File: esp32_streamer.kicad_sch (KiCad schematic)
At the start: 46 parts, among them J1 USB4510-03-1-A, J2 SJ1-3533NS, J3 Conn_01x04_Male, U1 PCM5122PW, U2 ESP32-WROVER-EM213EH2864PH3Q0, U3 MCP1825S, U4 MCP1825S

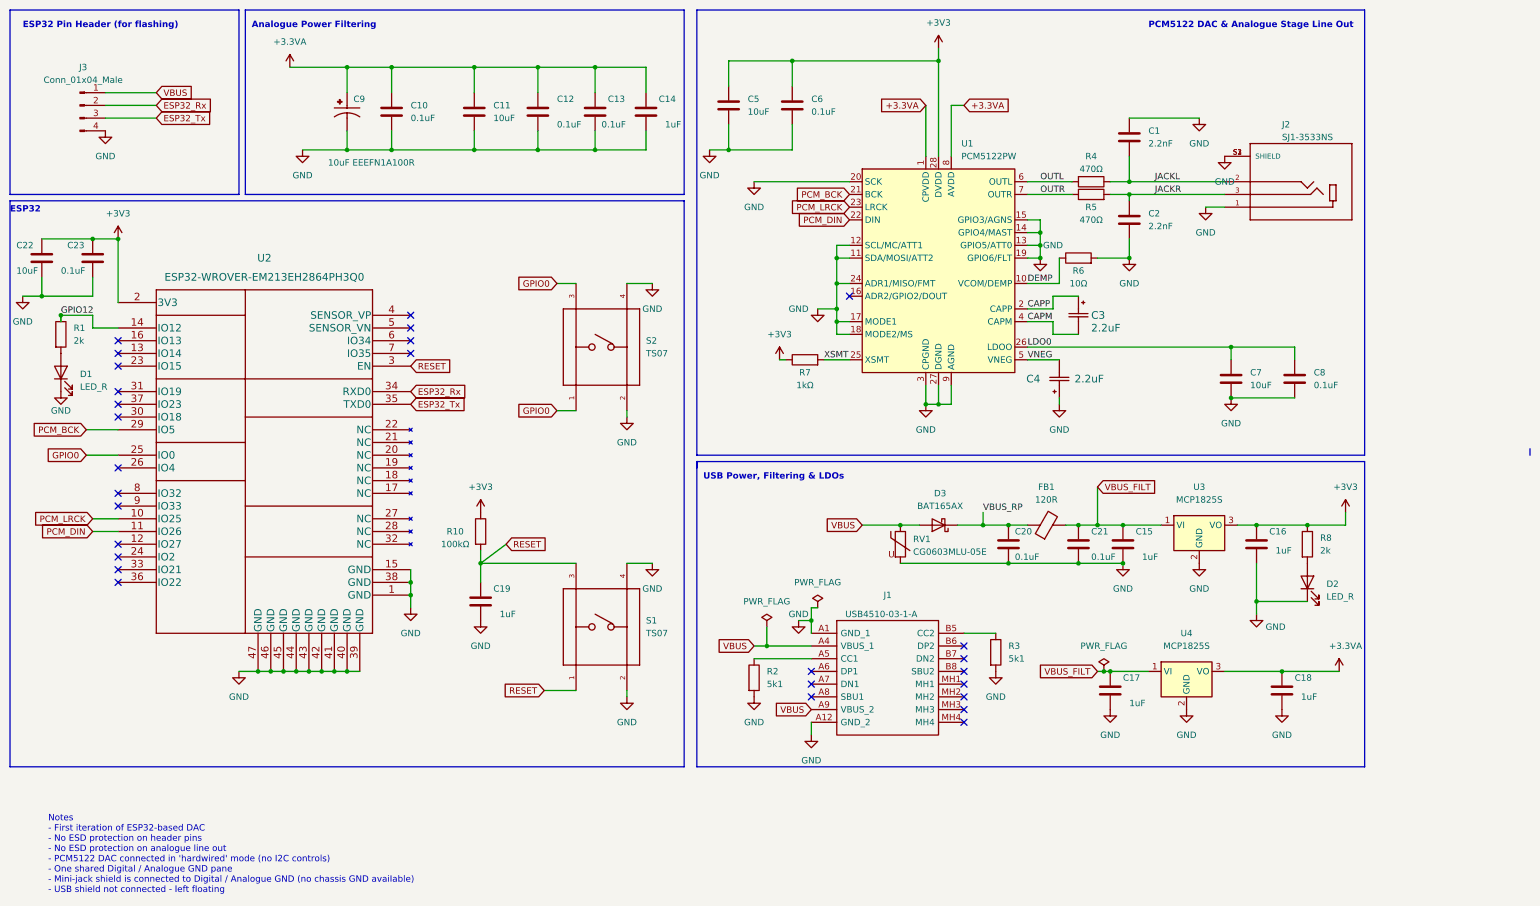
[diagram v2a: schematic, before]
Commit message: Updated PCB layout - now it looks cleaner - completed layout. next step: traces
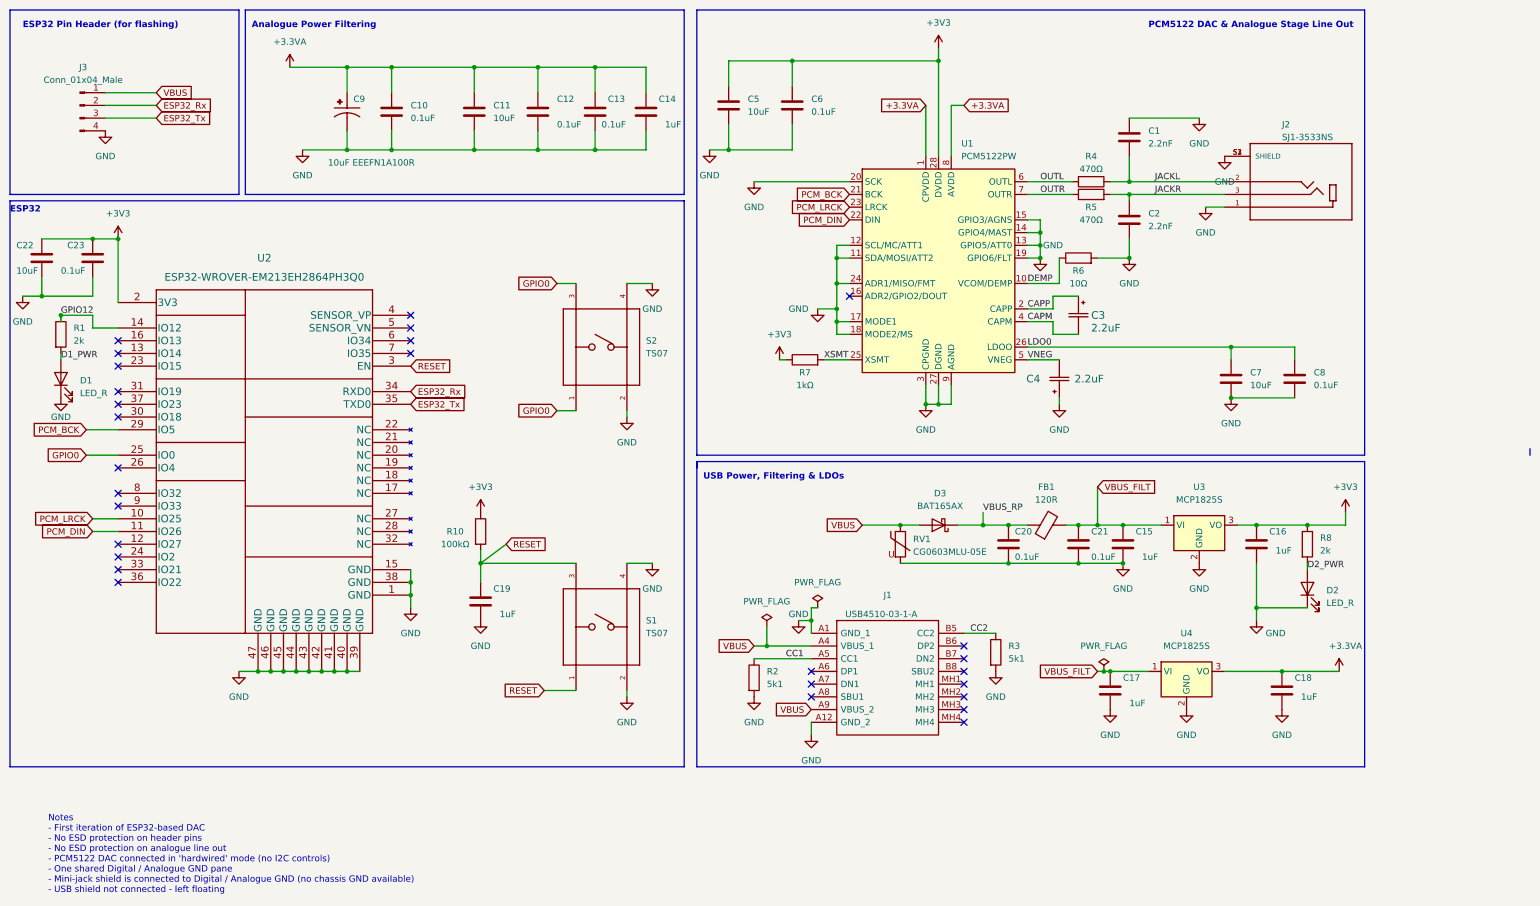
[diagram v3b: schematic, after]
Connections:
- net D2_PWR: now reaches D2.2 (A), R8.2
- net CC1: now reaches J1.A5 (CC1), R2.1
- net D1_PWR: now reaches D1.2 (A), R1.2
- net CC2: now reaches J1.B5 (CC2), R3.1
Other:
- moved on the sheet: D1, D2
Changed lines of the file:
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@@
   (junction (at 81.28 24.13) (diameter 0) (color 0 0 0 0)
   )
-  (junction (at 262.89 130.81) (diameter 0) (color 0 0 0 0)
+  (junction (at 262.89 132.08) (diameter 0) (color 0 0 0 0)
   )
   (junction (at 20.32 69.85) (diameter 0) (color 0 0 0 0)
@@
     (stroke (width 0) (type default) (color 0 0 0 0))
   )
-  (wire (pts (xy 262.89 130.81) (xy 262.89 133.35))
+  (wire (pts (xy 262.89 132.08) (xy 262.89 134.62))
     (stroke (width 0) (type default) (color 0 0 0 0))
   )
@@
     (stroke (width 0) (type default) (color 0 0 0 0))
   )
-  (wire (pts (xy 262.89 123.19) (xy 262.89 130.81))
+  (wire (pts (xy 262.89 123.19) (xy 262.89 132.08))
     (stroke (width 0) (type default) (color 0 0 0 0))
   )
@@
     (stroke (width 0) (type default) (color 0 0 0 0))
   )
-  (wire (pts (xy 262.89 130.81) (xy 273.05 130.81))
+  (wire (pts (xy 262.89 132.08) (xy 273.05 132.08))
     (stroke (width 0) (type default) (color 0 0 0 0))
   )
@@
     (stroke (width 0) (type default) (color 0 0 0 0))
   )
+  (wire (pts (xy 273.05 124.46) (xy 273.05 123.19))
+    (stroke (width 0) (type default) (color 0 0 0 0))
+  )
   (wire (pts (xy 153.67 40.64) (xy 157.48 40.64))
     (stroke (width 0) (type default) (color 0 0 0 0))
@@
   )
   (wire (pts (xy 119.38 40.64) (xy 119.38 36.83))
+    (stroke (width 0) (type default) (color 0 0 0 0))
+  )
+  (wire (pts (xy 24.13 82.55) (xy 24.13 81.28))
     (stroke (width 0) (type default) (color 0 0 0 0))
   )
@@
     (effects (font (size 1.27 1.27)) (justify left bottom))
   )
+  (label "CC2" (at 205.74 137.16 0)
+    (effects (font (size 1.27 1.27)) (justify left bottom))
+  )
+  (label "D2_PWR" (at 273.05 124.46 0)
+    (effects (font (size 1.27 1.27)) (justify left bottom))
+  )
   (label "DEMP" (at 217.17 67.31 0)
     (effects (font (size 1.27 1.27)) (justify left bottom))
@@
     (effects (font (size 1.27 1.27)) (justify left bottom))
   )
+  (label "D1_PWR" (at 24.13 82.55 0)
+    (effects (font (size 1.27 1.27)) (justify left bottom))
+  )
   (label "CAPM" (at 217.17 74.93 0)
     (effects (font (size 1.27 1.27)) (justify left bottom))
   )
   (label "XSMT" (at 176.53 82.55 0)
+    (effects (font (size 1.27 1.27)) (justify left bottom))
+  )
+  (label "CC1" (at 168.91 142.24 0)
     (effects (font (size 1.27 1.27)) (justify left bottom))
   )
@@
     (pin "2")
   )
-  (symbol (lib_id "power:GND") (at 24.13 88.9 0) (unit 1)
-    (in_bom yes) (on_board yes)
-    (property "Reference" "#PWR0129" (id 0) (at 24.13 95.25 0)
-      (effects (font (size 1.27 1.27)) hide)
-    )
-    (property "Value" "GND" (id 1) (at 24.13 92.71 0))
-    (property "Footprint" "" (id 2) (at 24.13 88.9 0)
-      (effects (font (size 1.27 1.27)) hide)
-    )
-    (property "Datasheet" "" (id 3) (at 24.13 88.9 0)
+  (symbol (lib_id "power:GND") (at 24.13 90.17 0) (unit 1)
+    (in_bom yes) (on_board yes)
+    (property "Reference" "#PWR0129" (id 0) (at 24.13 96.52 0)
+      (effects (font (size 1.27 1.27)) hide)
+    )
+    (property "Value" "GND" (id 1) (at 24.13 93.98 0))
+    (property "Footprint" "" (id 2) (at 24.13 90.17 0)
+      (effects (font (size 1.27 1.27)) hide)
+    )
+    (property "Datasheet" "" (id 3) (at 24.13 90.17 0)
       (effects (font (size 1.27 1.27)) hide)
     )
@@
     (pin "2")
   )
-  (symbol (lib_id "power:GND") (at 262.89 133.35 0) (unit 1)
-    (in_bom yes) (on_board yes)
-    (property "Reference" "#PWR0104" (id 0) (at 262.89 139.7 0)
-      (effects (font (size 1.27 1.27)) hide)
-    )
-    (property "Value" "GND" (id 1) (at 266.7 135.89 0))
-    (property "Footprint" "" (id 2) (at 262.89 133.35 0)
-      (effects (font (size 1.27 1.27)) hide)
-    )
-    (property "Datasheet" "" (id 3) (at 262.89 133.35 0)
+  (symbol (lib_id "power:GND") (at 262.89 134.62 0) (unit 1)
+    (in_bom yes) (on_board yes)
+    (property "Reference" "#PWR0104" (id 0) (at 262.89 140.97 0)
+      (effects (font (size 1.27 1.27)) hide)
+    )
+    (property "Value" "GND" (id 1) (at 266.7 137.16 0))
+    (property "Footprint" "" (id 2) (at 262.89 134.62 0)
+      (effects (font (size 1.27 1.27)) hide)
+    )
+    (property "Datasheet" "" (id 3) (at 262.89 134.62 0)
       (effects (font (size 1.27 1.27)) hide)
     )
@@
     (pin "MH4")
   )
-  (symbol (lib_id "Device:LED") (at 273.05 127 90) (unit 1)
-    (in_bom yes) (on_board yes) (fields_autoplaced)
-    (property "Reference" "D2" (id 0) (at 276.86 127.3174 90)
+  (symbol (lib_id "Device:LED") (at 273.05 128.27 90) (unit 1)
+    (in_bom yes) (on_board yes) (fields_autoplaced)
+    (property "Reference" "D2" (id 0) (at 276.86 128.5874 90)
       (effects (font (size 1.27 1.27)) (justify right))
     )
-    (property "Value" "LED_R" (id 1) (at 276.86 129.8574 90)
+    (property "Value" "LED_R" (id 1) (at 276.86 131.1274 90)
       (effects (font (size 1.27 1.27)) (justify right))
     )
-    (property "Footprint" "LED_SMD:LED_0603_1608Metric" (id 2) (at 273.05 127 0)
-      (effects (font (size 1.27 1.27)) hide)
-    )
-    (property "Datasheet" "~" (id 3) (at 273.05 127 0)
+    (property "Footprint" "LED_SMD:LED_0603_1608Metric" (id 2) (at 273.05 128.27 0)
+      (effects (font (size 1.27 1.27)) hide)
+    )
+    (property "Datasheet" "~" (id 3) (at 273.05 128.27 0)
       (effects (font (size 1.27 1.27)) hide)
     )
@@
     (pin "1")
   )
-  (symbol (lib_id "Device:LED") (at 24.13 85.09 90) (unit 1)
-    (in_bom yes) (on_board yes) (fields_autoplaced)
-    (property "Reference" "D1" (id 0) (at 27.94 85.4074 90)
+  (symbol (lib_id "Device:LED") (at 24.13 86.36 90) (unit 1)
+    (in_bom yes) (on_board yes) (fields_autoplaced)
+    (property "Reference" "D1" (id 0) (at 27.94 86.6774 90)
       (effects (font (size 1.27 1.27)) (justify right))
     )
-    (property "Value" "LED_R" (id 1) (at 27.94 87.9474 90)
+    (property "Value" "LED_R" (id 1) (at 27.94 89.2174 90)
       (effects (font (size 1.27 1.27)) (justify right))
     )
-    (property "Footprint" "LED_SMD:LED_0603_1608Metric" (id 2) (at 24.13 85.09 0)
-      (effects (font (size 1.27 1.27)) hide)
-    )
-    (property "Datasheet" "~" (id 3) (at 24.13 85.09 0)
-      (effects (font (size 1.27 1.27)) hide)
-    )
+    (property "Footprint" "LED_SMD:LED_0603_1608Metric" (id 2) (at 24.13 86.36 0)
+      (effects (font (size 1.27 1.27)) hide)
+    )
+    (property "Datasheet" "~" (id 3) (at 24.13 86.36 0)
+      (effects (font (size 1.27 1.27)) hide)
+    )
